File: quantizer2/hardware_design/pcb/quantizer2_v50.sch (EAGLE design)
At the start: 54 parts, among them IC2 LM4040C10IDBZR, IC3 LM1117DT-3.3_NOPB, IC4 MCP3201-CI_MS, IC5 MCP4921T-E_MS, IC9 TL072CD, U1 LM4040C25IDBZR, Y1 8MHz

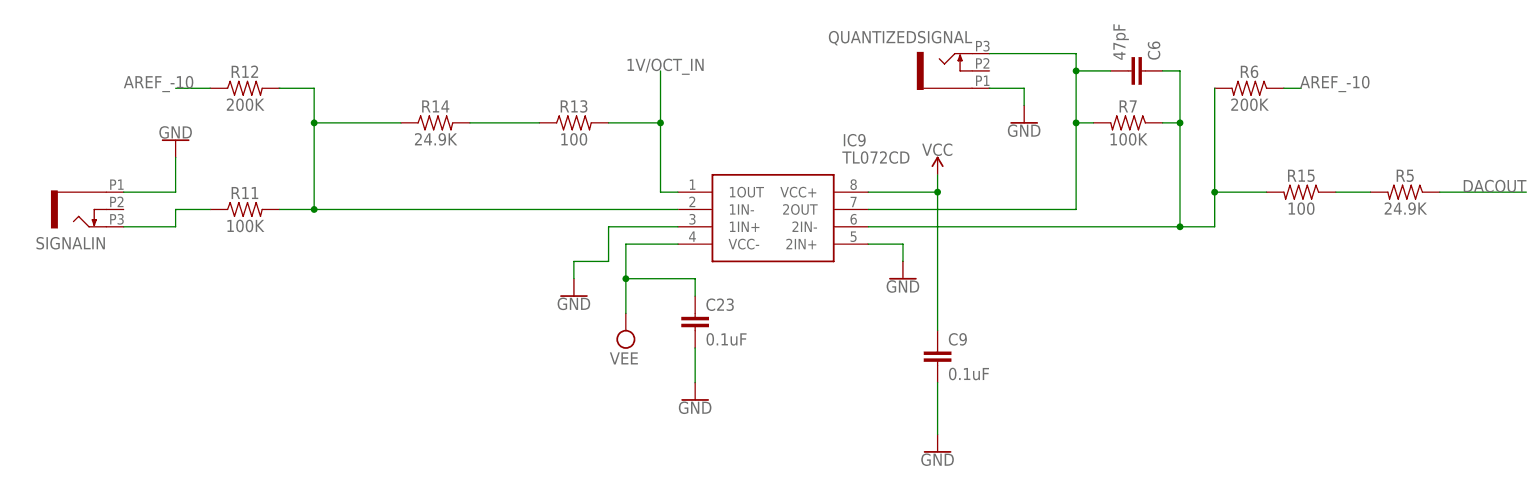
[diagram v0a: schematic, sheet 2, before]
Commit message: progress on audio DAC. switched to f446xx for now
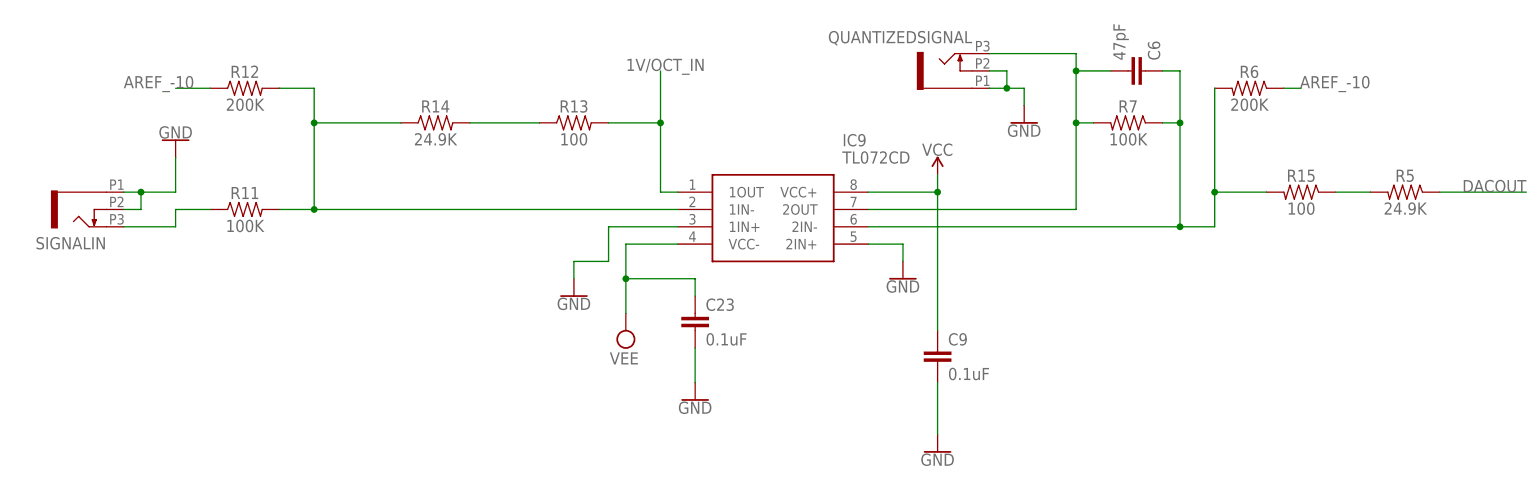
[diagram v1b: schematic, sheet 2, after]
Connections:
- net GND: now also QUANTIZEDSIGNAL.2, SIGNALIN.2
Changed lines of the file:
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@@
 <segment>
 <pinref part="QUANTIZEDSIGNAL" gate="G$1" pin="1"/>
-<wire x1="149.86" y1="223.52" x2="154.94" y2="223.52" width="0.1524" layer="91"/>
+<wire x1="149.86" y1="223.52" x2="152.4" y2="223.52" width="0.1524" layer="91"/>
 <pinref part="GND8" gate="1" pin="GND"/>
+<wire x1="152.4" y1="223.52" x2="154.94" y2="223.52" width="0.1524" layer="91"/>
 <wire x1="154.94" y1="223.52" x2="154.94" y2="220.98" width="0.1524" layer="91"/>
+<pinref part="QUANTIZEDSIGNAL" gate="G$1" pin="2"/>
+<wire x1="149.86" y1="226.06" x2="152.4" y2="226.06" width="0.1524" layer="91"/>
+<wire x1="152.4" y1="226.06" x2="152.4" y2="223.52" width="0.1524" layer="91"/>
+<junction x="152.4" y="223.52"/>
 </segment>
 <segment>
 <pinref part="SIGNALIN" gate="G$1" pin="1"/>
-<wire x1="22.86" y1="208.28" x2="30.48" y2="208.28" width="0.1524" layer="91"/>
+<wire x1="22.86" y1="208.28" x2="25.4" y2="208.28" width="0.1524" layer="91"/>
 <pinref part="GND7" gate="1" pin="GND"/>
+<wire x1="25.4" y1="208.28" x2="30.48" y2="208.28" width="0.1524" layer="91"/>
 <wire x1="30.48" y1="208.28" x2="30.48" y2="213.36" width="0.1524" layer="91"/>
+<pinref part="SIGNALIN" gate="G$1" pin="2"/>
+<wire x1="22.86" y1="205.74" x2="25.4" y2="205.74" width="0.1524" layer="91"/>
+<wire x1="25.4" y1="205.74" x2="25.4" y2="208.28" width="0.1524" layer="91"/>
+<junction x="25.4" y="208.28"/>
 </segment>
 <segment>
